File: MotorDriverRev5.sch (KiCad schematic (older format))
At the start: 114 parts, among them J10 n/a, J15 Board_hole, J16 Board_hole, J17 Board_hole, J18 Board_hole, J19 Board_hole, J20 Board_hole, J3 Intel_LGA115x_holes, J5 CONN_01X06, J6 N/A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

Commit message: test
testing github
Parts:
- Q6: Distrib PN IRF6662TRPBFCT-ND -> fadfasdf
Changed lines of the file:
@@
 LIBS:valves
 LIBS:diode
-LIBS:Kicad_components_LJD
 LIBS:MotorDriverRev5-cache
 EELAYER 25 0
@@
 F 4 "Infineon" H 18100 9300 60  0001 C CNN "MFG Name"
 F 5 "IRF6662TRPBF	" H 17750 9200 60  0001 C CNN "MFG Part #"
-F 6 "IRF6662TRPBFCT-ND" H 17900 9000 60  0001 C CNN "Distrib PN"
+F 6 "fadfasdf" H 17900 9000 60  0001 C CNN "Distrib PN"
 F 7 "http://www.digikey.com/product-detail/en/IRF6662TRPBF/IRF6662TRPBFCT-ND/1189872" H 19400 9100 60  0001 C CNN "Distrib Link"
 	1    19800 8150

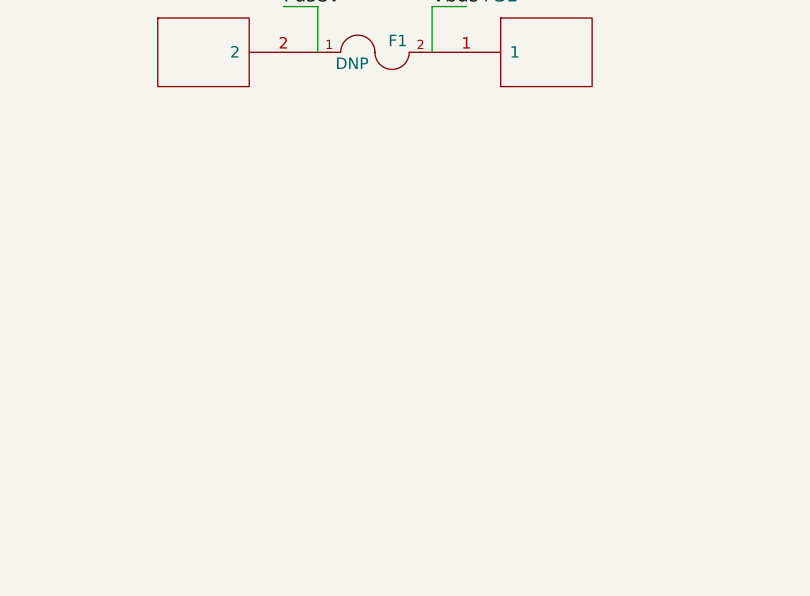
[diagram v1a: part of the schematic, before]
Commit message: began buck converter (test)
added a mosfet, diode, and inductor underneath the power supply portion
of the schematic
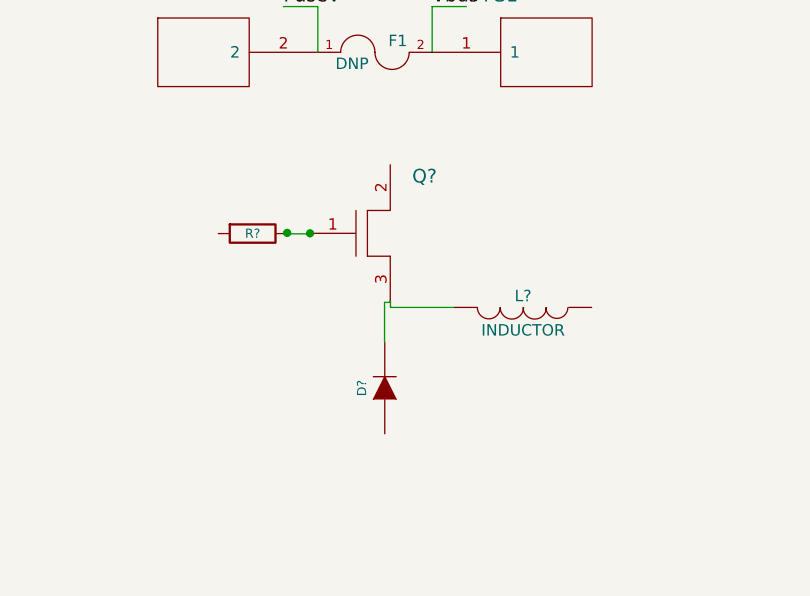
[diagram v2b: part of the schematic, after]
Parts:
- added D?: Diode, LJD_Footprints:SOD-323, symbol DIODE
- added L?: INDUCTOR, symbol INDUCTOR
- added Q?: FET_small, LJD_footprints:DirectFETMZ, symbol FET_small
- added R?: 2R2, 0805 1%, 1/8W, Resistors_SMD:R_0805, symbol R
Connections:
- wire segments 306 -> 313
